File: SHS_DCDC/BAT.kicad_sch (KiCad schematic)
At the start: 21 parts, among them Q10 PMV100XPEAR, Q11 PMV100XPEAR, Q12 PMV100XPEAR, Q13 PMV100XPEAR, Q17 PMV100XPEAR, Q20 BSS84, Q21 2N7002, Q9 PMV100XPEAR, U2 INA181, U7 MCP101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

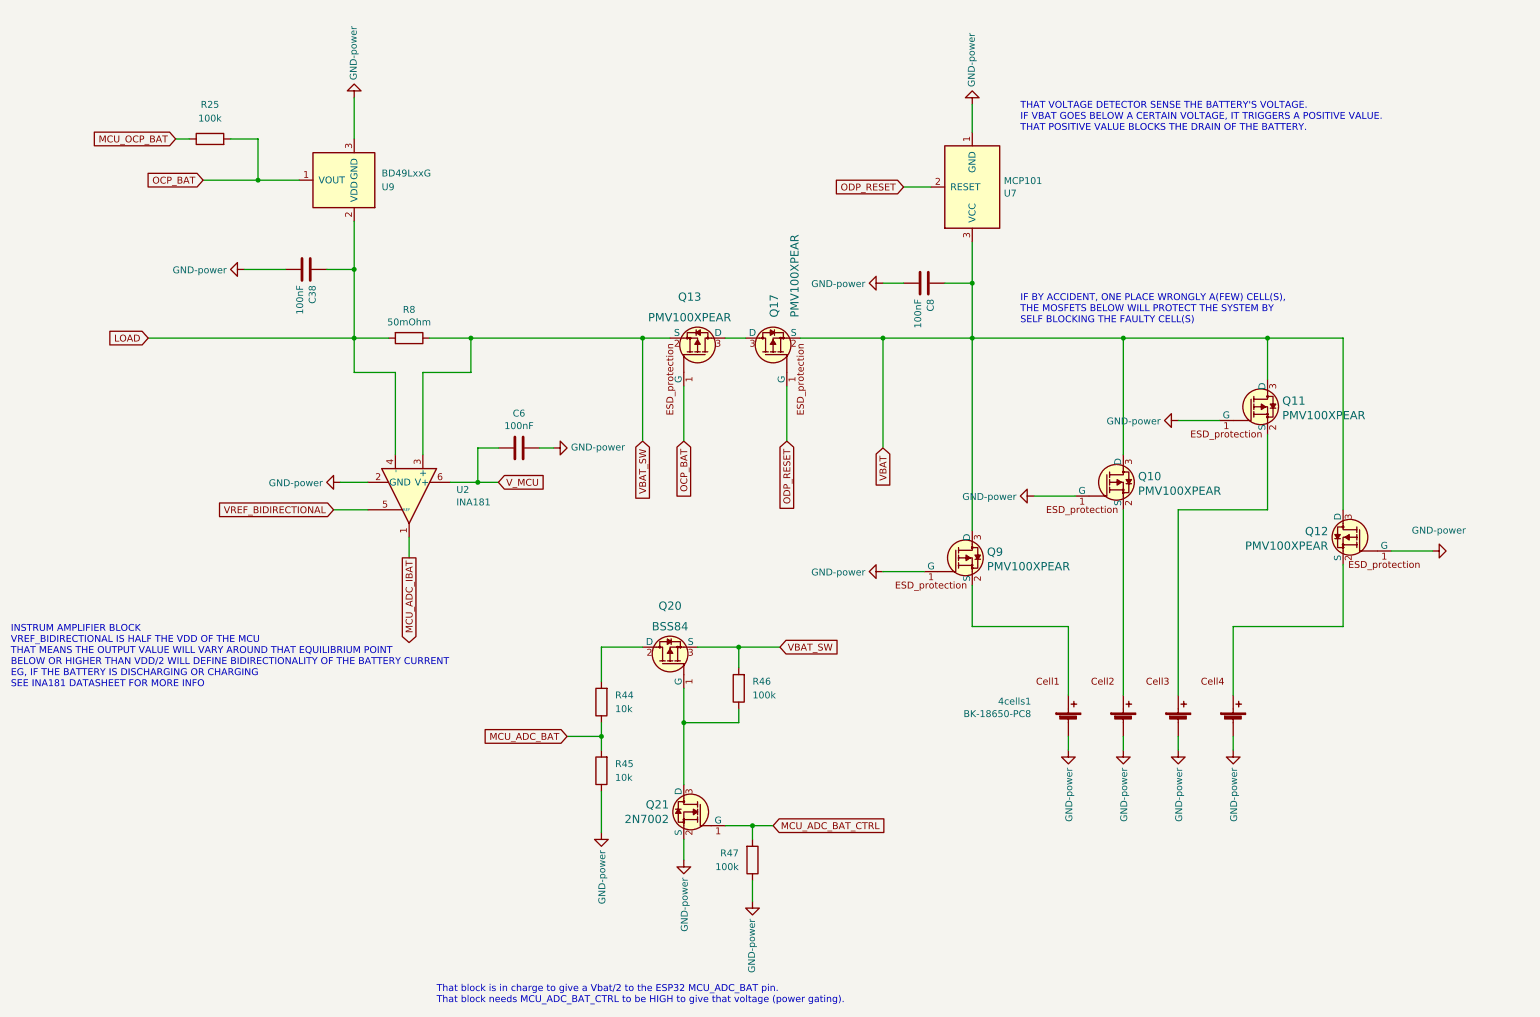
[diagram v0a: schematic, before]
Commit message: DFU update
PCB update to setup 3 ways of FW/Debug capability:
1. JTAG (FW & Debug)
2. USB DFU (FW & Debug)
3. UART (FW only)
With BOOT0 button installed too
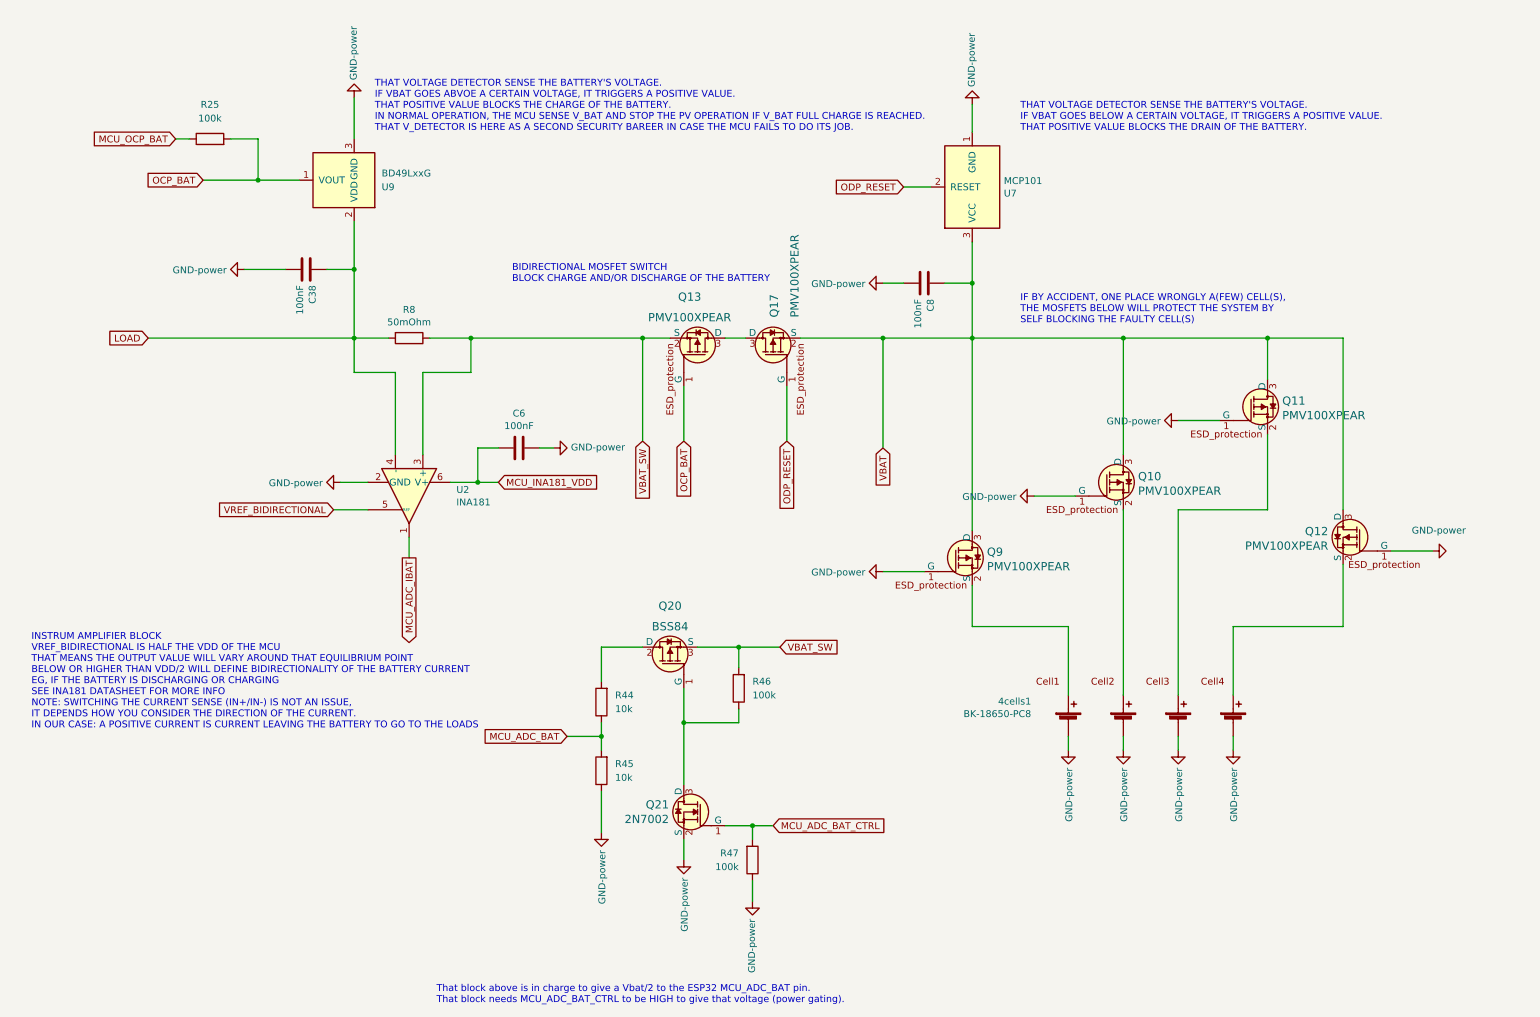
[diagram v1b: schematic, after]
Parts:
- C6: footprint Capacitor_SMD:C_0603_1608Metric -> Capacitor_SMD:C_0402_1005Metric
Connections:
- net V_MCU renamed MCU_INA181_VDD
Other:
- note added: "BIDIRECTIONAL MOSFET SWITCH BLOCK CHARGE AND/OR DISCHARGE OF THE BATTERY"
- note added: "INSTRUM AMPLIFIER BLOCK VREF_BIDIRECTIONAL IS HALF THE VDD OF THE MCU THAT MEANS THE OUTPUT VALUE WILL VARY AROUND THAT EQUILIBRIUM POINT BELOW OR HIGHER THAN VDD/2 WILL DEFINE BIDIRECTIONALITY OF THE BATTERY CURRENT EG, IF THE BATTERY IS DISCHARGING OR CHARGING SEE INA181 DATASHEET FOR MORE INFO NOTE: SWITCHING THE CURRENT SENSE (IN+/IN-) IS NOT AN ISSUE, IT DEPENDS HOW YOU CONSIDER THE DIRECTIO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"
- note added: "THAT VOLTAGE DETECTOR SENSE THE BATTERY'S VOLTAGE. IF VBAT GOES ABVOE A CERTAIN VOLTAGE, IT TRIGGERS A POSITIVE VALUE. THAT POSITIVE VALUE BLOCKS THE CHARGE OF THE BATTERY. IN NORMAL OPERATION, THE MCU SENSE V_BAT AND STOP THE PV OPERATION IF V_BAT FULL CHARGE IS REACHED. THAT V_DETECTOR IS HERE AS A SECOND SECURITY BAREER IN CASE THE MCU FAILS TO DO ITS JOB."
- note added: "That block above is in charge to give a Vbat/2 to the ESP32 MCU_ADC_BAT pin. That block needs MCU_ADC_BAT_CTRL to be HIGH to give that voltage (power gating)."
- note removed: "INSTRUM AMPLIFIER BLOCK VREF_BIDIRECTIONAL IS HALF THE VDD OF THE MCU THAT MEANS THE OUTPUT VALUE WILL VARY AROUND THAT EQUILIBRIUM POINT BELOW OR HIGHER THAN VDD/2 WILL DEFINE BIDIRECTIONALITY OF THE BATTERY CURRENT EG, IF THE BATTERY IS DISCHARGING OR CHARGING SEE INA181 DATASHEET FOR MORE INFO"
- note removed: "That block is in charge to give a Vbat/2 to the ESP32 MCU_ADC_BAT pin. That block needs MCU_ADC_BAT_CTRL to be HIGH to give that voltage (power gating)."
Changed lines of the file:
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@@
+    (effects (font (size 1.27 1.27)) (justify left bottom))
+  )
+  (text "BIDIRECTIONAL MOSFET SWITCH\nBLOCK CHARGE AND/OR DISCHARGE OF THE BATTERY"
+    (at 105.41 62.23 0)
     (effects (font (size 1.27 1.27)) (justify left bottom))
   )
@@
     (effects (font (size 1.27 1.27)) (justify left bottom))
   )
-  (text "That block is in charge to give a Vbat/2 to the ESP32 MCU_ADC_BAT pin.\nThat block needs MCU_ADC_BAT_CTRL to be HIGH to give that voltage (power gating)."
+  (text "That block above is in charge to give a Vbat/2 to the ESP32 MCU_ADC_BAT pin.\nThat block needs MCU_ADC_BAT_CTRL to be HIGH to give that voltage (power gating)."
     (at 91.44 195.58 0)
     (effects (font (size 1.27 1.27)) (justify left bottom))
   )
-  (text "INSTRUM AMPLIFIER BLOCK\nVREF_BIDIRECTIONAL IS HALF THE VDD OF THE MCU\nTHAT MEANS THE OUTPUT VALUE WILL VARY AROUND THAT EQUILIBRIUM POINT\nBELOW OR HIGHER THAN VDD/2 WILL DEFINE BIDIRECTIONALITY OF THE BATTERY CURRENT\nEG, IF THE BATTERY IS DISCHARGING OR CHARGING\nSEE INA181 DATASHEET FOR MORE INFO"
-    (at 12.7 137.16 0)
+  (text "THAT VOLTAGE DETECTOR SENSE THE BATTERY'S VOLTAGE.\nIF VBAT GOES ABVOE A CERTAIN VOLTAGE, IT TRIGGERS A POSITIVE VALUE.\nTHAT POSITIVE VALUE BLOCKS THE CHARGE OF THE BATTERY.\nIN NORMAL OPERATION, THE MCU SENSE V_BAT AND STOP THE PV OPERATION IF V_BAT FULL CHARGE IS REACHED.\nTHAT V_DETECTOR IS HERE AS A SECOND SECURITY BAREER IN CASE THE MCU FAILS TO DO ITS JOB."
+    (at 80.01 34.29 0)
+    (effects (font (size 1.27 1.27)) (justify left bottom))
+  )
+  (text "INSTRUM AMPLIFIER BLOCK\nVREF_BIDIRECTIONAL IS HALF THE VDD OF THE MCU\nTHAT MEANS THE OUTPUT VALUE WILL VARY AROUND THAT EQUILIBRIUM POINT\nBELOW OR HIGHER THAN VDD/2 WILL DEFINE BIDIRECTIONALITY OF THE BATTERY CURRENT\nEG, IF THE BATTERY IS DISCHARGING OR CHARGING\nSEE INA181 DATASHEET FOR MORE INFO\nNOTE: SWITCHING THE CURRENT SENSE (IN+/IN-) IS NOT AN ISSUE,\nIT DEPENDS HOW YOU CONSIDER THE DIRECTION OF THE CURRENT.\nIN OUR CASE: A POSITIVE CURRENT IS CURRENT LEAVING THE BATTERY TO GO TO THE LOADS"
+    (at 16.51 144.78 0)
     (effects (font (size 1.27 1.27)) (justify left bottom))
   )
@@
     )
   )
-  (global_label "V_MCU" (shape input) (at 102.87 99.06 0) (fields_autoplaced)
+  (global_label "MCU_INA181_VDD" (shape input) (at 102.87 99.06 0) (fields_autoplaced)
     (effects (font (size 1.27 1.27)) (justify left))
-    (property "Intersheet References" "${INTERSHEET_REFS}" (id 0) (at -10.16 294.64 0)
-      (effects (font (size 1.27 1.27)) hide)
+    (property "Intersheet References" "${INTERSHEET_REFS}" (id 0) (at 121.4623 98.9806 0)
+      (effects (font (size 1.27 1.27)) (justify left) hide)
     )
   )
@@
     (property "Reference" "C6" (id 0) (at 106.68 86.3092 90))
     (property "Value" "100nF" (id 1) (at 106.68 88.6206 90))
-    (property "Footprint" "Capacitor_SMD:C_0603_1608Metric" (id 2) (at 102.87 93.6752 0)
+    (property "Footprint" "Capacitor_SMD:C_0402_1005Metric" (id 2) (at 102.87 93.6752 0)
       (effects (font (size 1.27 1.27)) hide)
     )

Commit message: Final_check stage
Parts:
- removed U7: MCP101, Package_TO_SOT_SMD:SOT-23, symbol SHS_DCDC:MCP101
- added U6: APX810SA, Package_TO_SOT_SMD:SOT-23, symbol SHS_DCDC:APX810SA
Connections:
- net GND: now also U6.1 (GND)
- net ODP_RESET: now also U6.2 (RESET)
- net VBAT: now also Q20.3 (S), R46.2, U6.3 (VCC)
- net VBAT_SW: no longer names the net of Q13.2 (S), R8.1, U2.3 (+)
- net VBAT_SW: no longer Q20.3 (S), R46.2
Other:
- note added: "THAT VOLTAGE DETECTOR SENSE THE BATTERY'S VOLTAGE. IT IS TO DETECT AN OVER DISCHARGE VOLTAGE CONDITION. IF VBAT GOES BELOW A CERTAIN VOLTAGE, IT TRIGGERS A POSITIVE VALUE. THAT POSITIVE VALUE BLOCKS THE DRAIN OF THE BATTERY BY TURNING OFF A PMOS."
- note added: "THAT VOLTAGE DETECTOR SENSE THE BATTERY'S VOLTAGE. IT IS TO DETECT OVER CHARGE VOLTAGE CONDITION. IF VBAT GOES ABOVE A CERTAIN VOLTAGE, IT TRIGGERS A POSITIVE VALUE. THAT POSITIVE VALUE BLOCKS THE CHARGE OF THE BATTERY BY TURNING OFF A PMOS. IN NORMAL OPERATION, THE MCU SENSE V_BAT AND STOP THE PV OPERATION IF V_BAT FULL CHARGE IS REACHED. THAT V_DETECTOR ACTS HERE AS A SECOND SECURITY BAREER IN 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"
- note removed: "THAT VOLTAGE DETECTOR SENSE THE BATTERY'S VOLTAGE. IF VBAT GOES ABVOE A CERTAIN VOLTAGE, IT TRIGGERS A POSITIVE VALUE. THAT POSITIVE VALUE BLOCKS THE CHARGE OF THE BATTERY. IN NORMAL OPERATION, THE MCU SENSE V_BAT AND STOP THE PV OPERATION IF V_BAT FULL CHARGE IS REACHED. THAT V_DETECTOR IS HERE AS A SECOND SECURITY BAREER IN CASE THE MCU FAILS TO DO ITS JOB."
- note removed: "THAT VOLTAGE DETECTOR SENSE THE BATTERY'S VOLTAGE. IF VBAT GOES BELOW A CERTAIN VOLTAGE, IT TRIGGERS A POSITIVE VALUE. THAT POSITIVE VALUE BLOCKS THE DRAIN OF THE BATTERY."
- moved on the sheet: Q17

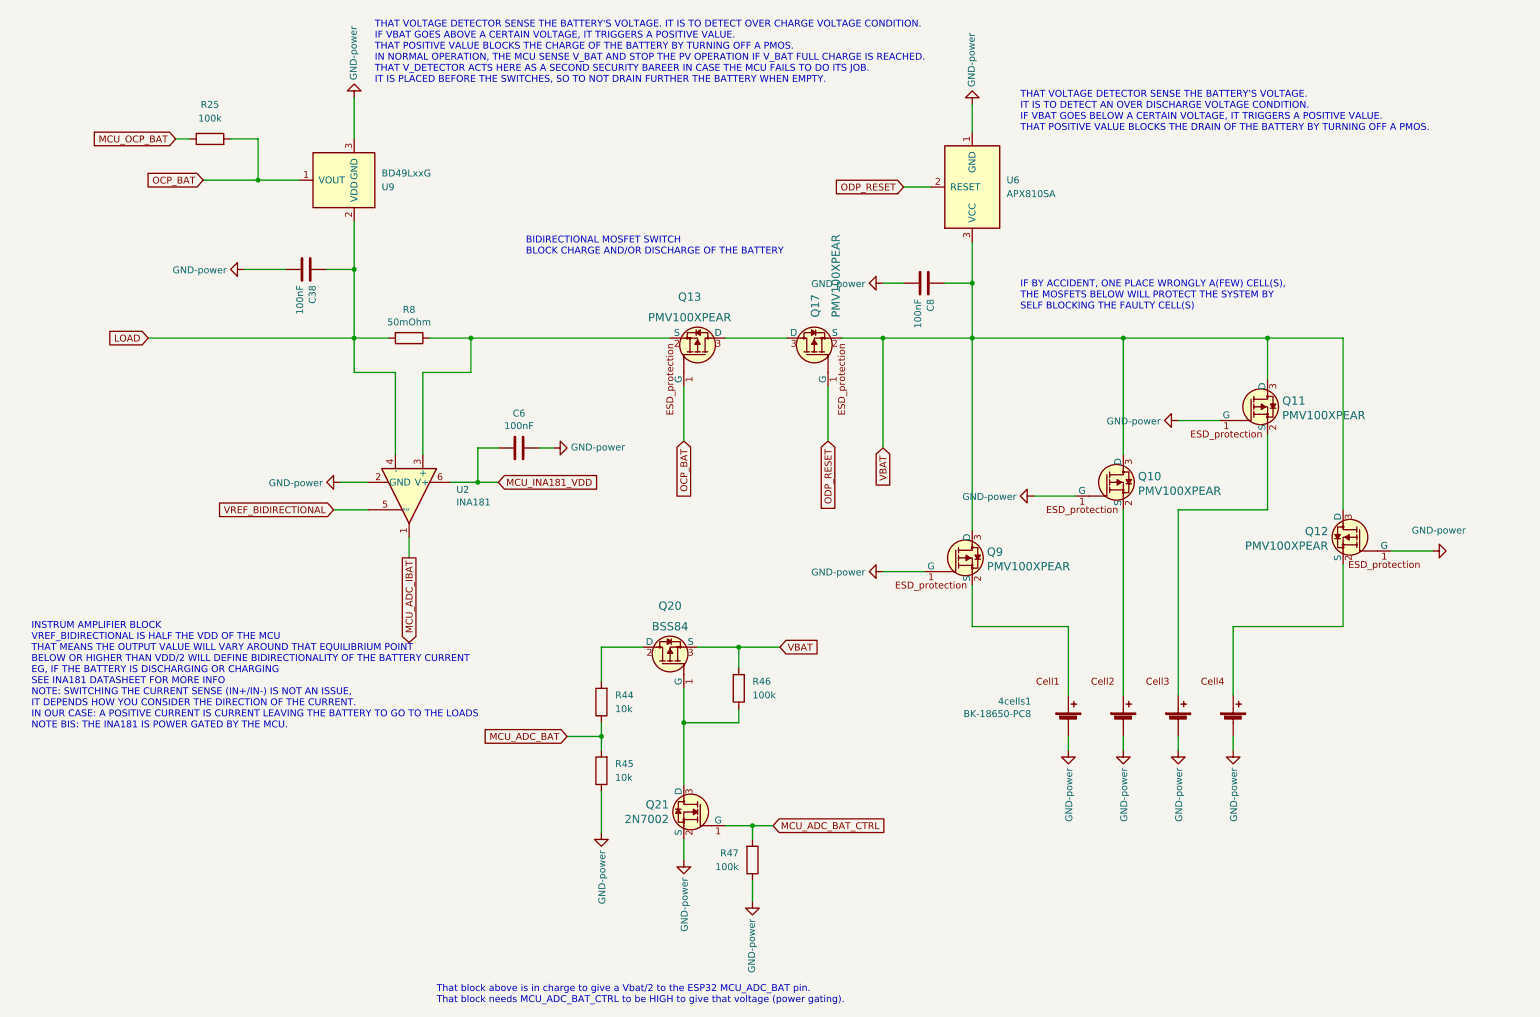
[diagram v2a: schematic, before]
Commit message: Testpoints
All the tests points have been placed
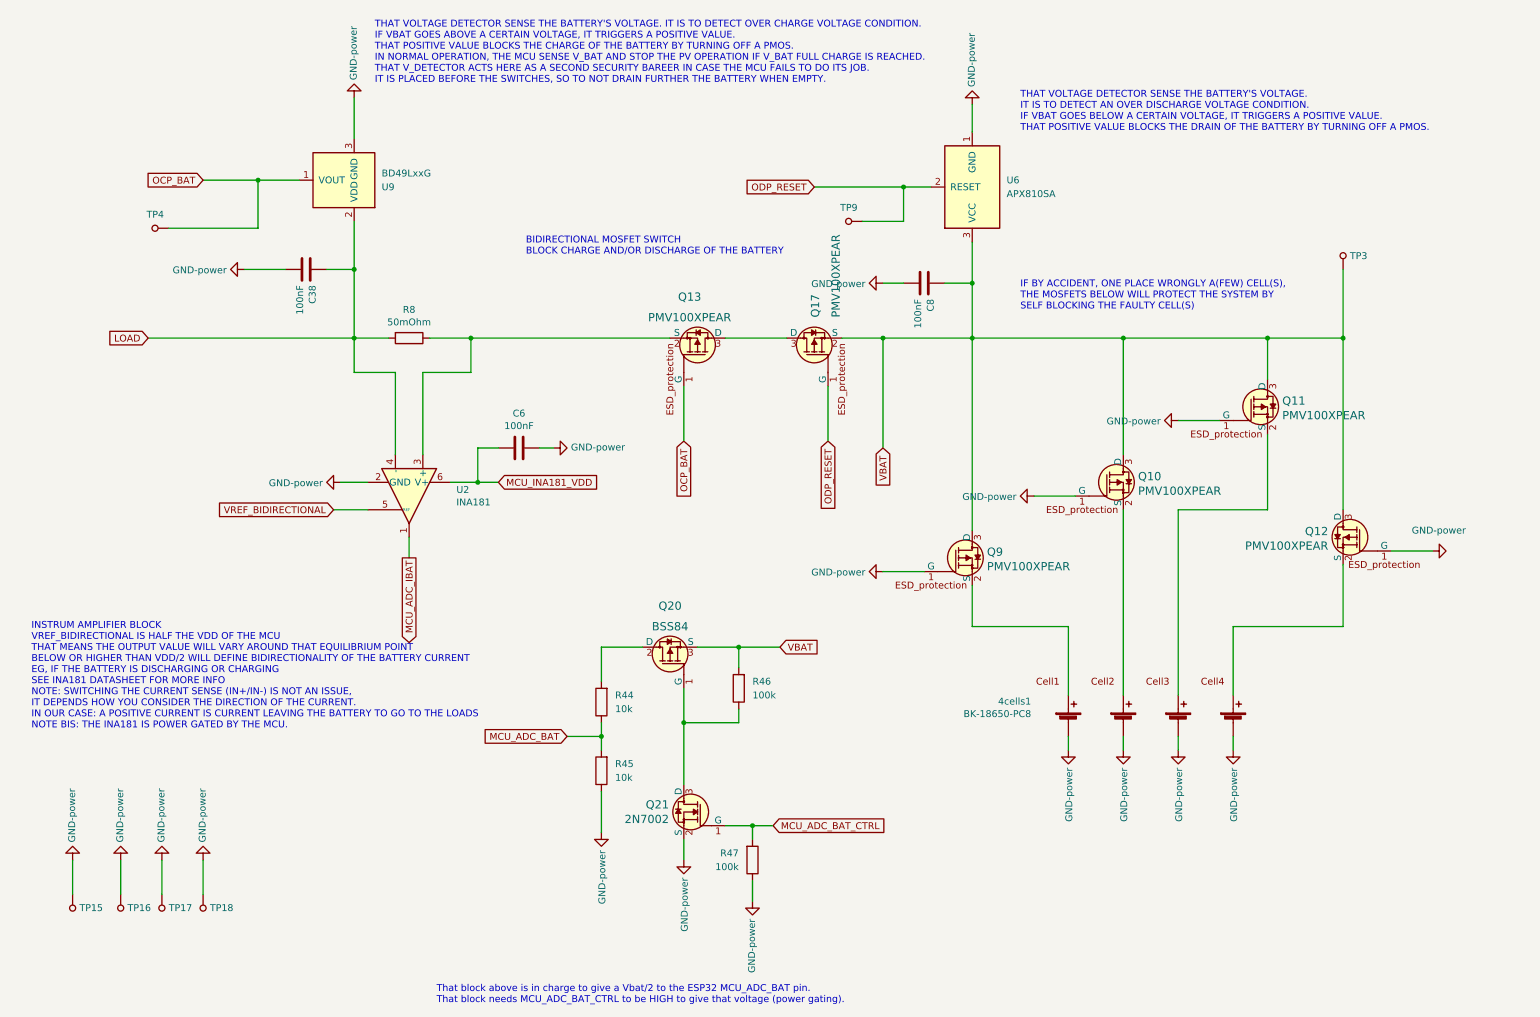
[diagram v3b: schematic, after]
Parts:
- removed R25: 100k, Resistor_SMD:R_0402_1005Metric, symbol Device:R
- added TP15, TP16, TP17, TP18, TP3, TP4, TP9: 5029, digikey-footprints:PC_Test_Point_Mini_3.8x2.03mm, symbol dk_Test-Points:5029
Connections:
- net GND: now also TP15.1, TP16.1, TP17.1, TP18.1
- net OCP_BAT: now also TP4.1
- net ODP_RESET: now also TP9.1
- net VBAT: now also TP3.1
